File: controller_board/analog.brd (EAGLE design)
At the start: 121 x 115.3 mm, 111 parts

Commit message: Pull commit
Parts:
- moved C27 0.32 mm to (37.1, 63.8)
- moved C28 0.32 mm to (39.7, 63.8)
- moved U$13 0.32 mm to (38.4, 58.4)
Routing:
- net N$30: track 30.9 -> 34.0 mm
- net +15V: track 349.2 -> 352.2 mm
- net N$24: track 28.1 -> 29.8 mm
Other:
- board text added: "Rev. 3 Bottom"
- board text added: "Rev. 3 Top"
- board text removed: "Rev. 2 Bottom"
- board text removed: "Rev. 2 Top"

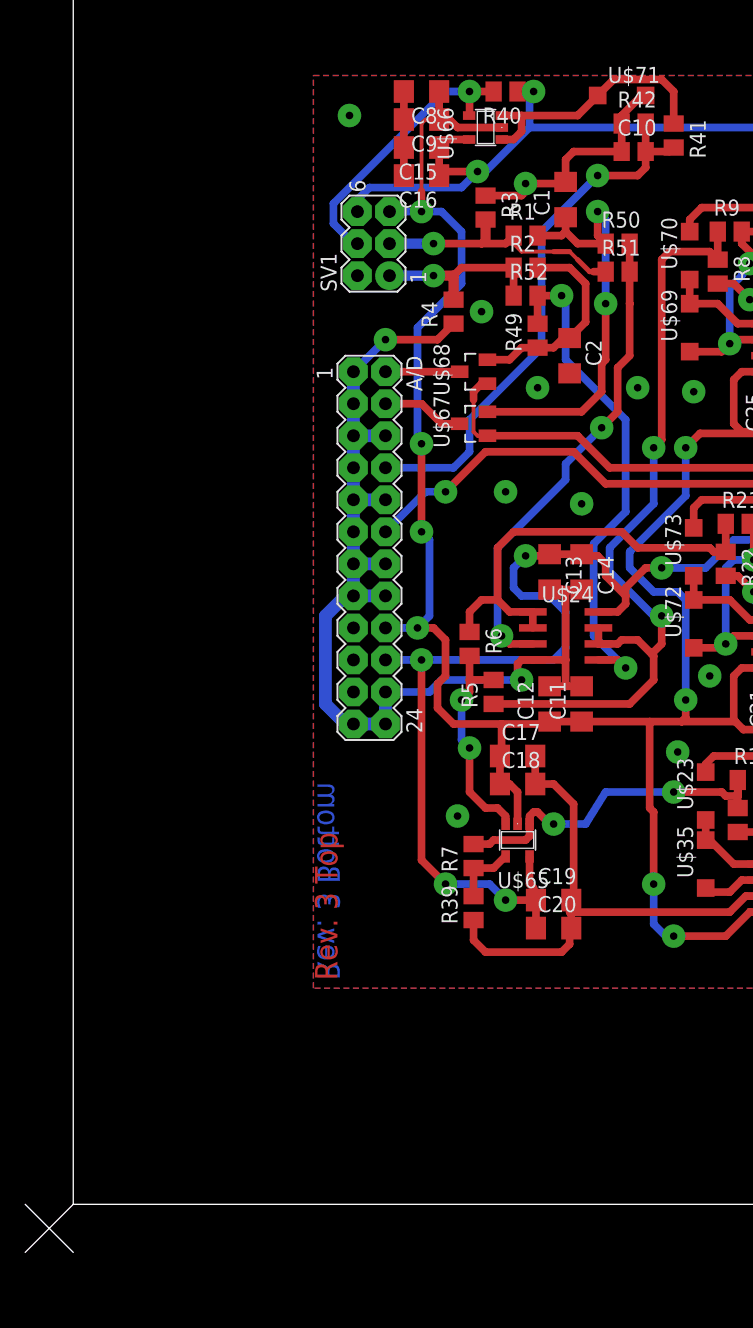
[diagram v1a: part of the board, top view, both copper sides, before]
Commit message: Little bit of writing, little bit of simulations. Lots of analog board work, but that's not evident here.
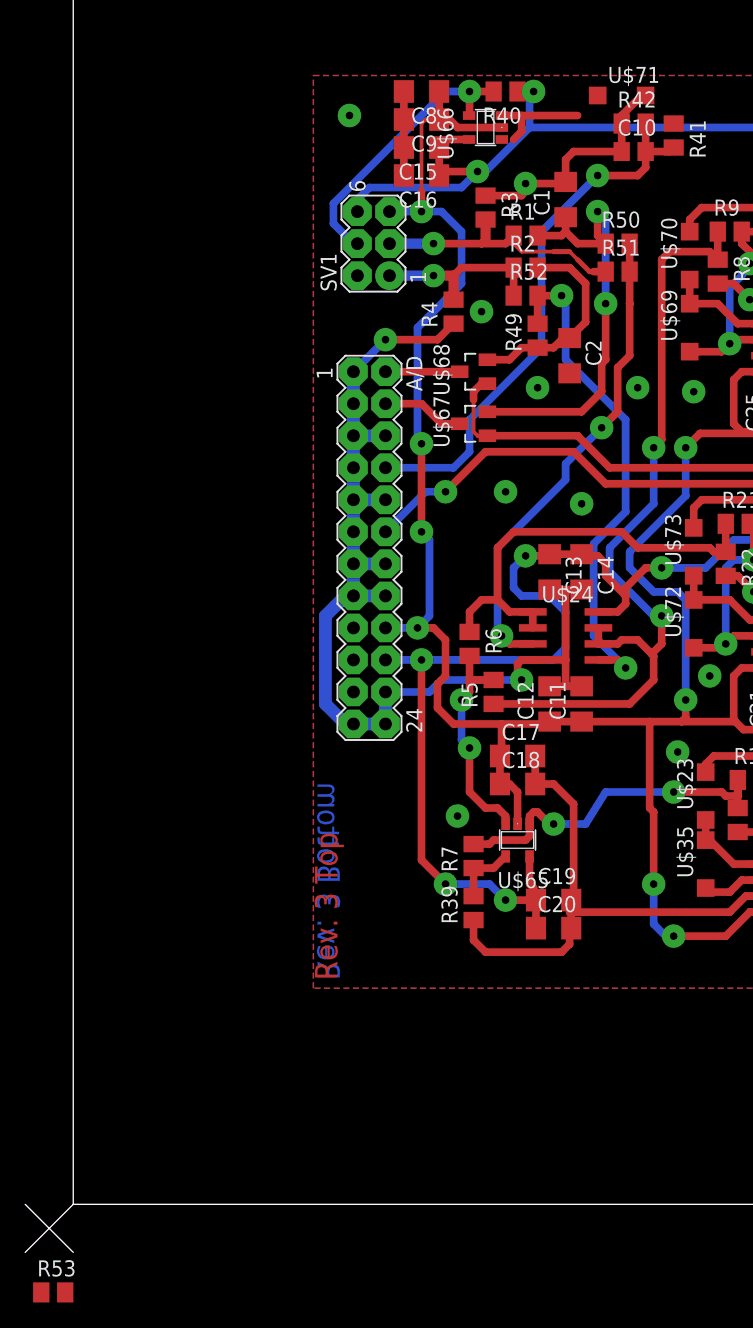
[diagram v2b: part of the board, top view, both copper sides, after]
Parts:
- added R53: 8k6, rcl:M0805
- C10: value (none) -> 330n
- R40: value (none) -> 11k
- R41: value (none) -> 43k
- R42: value (none) -> 10k
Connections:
- new net N$45: R41.1, R53.2, U$71.C
- net N$37: now also R53.1; no longer R41.1, U$71.C
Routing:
- net N$37: track 20.9 -> 8.18 mm
